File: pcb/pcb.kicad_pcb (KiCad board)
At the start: 2 copper layers, 34 parts, among them J1 USB_C_Receptacle_USB2.0_16P, J2 TC2030_SWD, J3 Conn_01x02_MountingPin, J4 Conn_01x04_MountingPin, SW1 SW_SPDT, SW2 RST, SW3 Kailh_Choc, SW4 Kailh_Choc, SW5 Kailh_Choc, SW6 Kailh_Choc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

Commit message: routing is hard
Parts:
- removed J2: TC2030_SWD, PCM_marbastlib-various:CON_TC2030_outlined
- J4: value Conn_01x04_MountingPin -> Conn_02x03_Odd_Even; footprint Connector_JST:JST_SH_SM04B-SRSS-TB_1x04-1MP_P1.00mm_Horizontal -> Connector_PinHeader_2.54mm:PinHeader_2x03_P2.54mm_Vertical
- moved F1 74.6 mm to (88.2, 51.6)
- moved FB2 71.3 mm to (86.4, 49.3), turned to -90 degrees
- moved SW3 69.4 mm to (30.0, 51.0)
- moved D1 68.7 mm to (92.4, 52.8), turned to -90 degrees
- moved SW6 67.4 mm to (30.0, 68.0)
- moved FB1 65.7 mm to (86.9, 53.6)
- moved U2 58.2 mm to (80.5, 52.5), turned to 180 degrees
- moved SW7 55.9 mm to (48.0, 68.0)
- moved SW8 53.7 mm to (66.0, 68.0)
- moved J4 46.4 mm to (96.4, 62.6)
- moved U1 43.7 mm to (86.8, 66.8)
- moved SW1 41.2 mm to (106.7, 56.0), turned to 90 degrees
- moved J1 39.8 mm to (80.5, 45.5), turned to 180 degrees
- moved R1 36.3 mm to (76.5, 52.5), turned to -90 degrees
- moved J3 34.1 mm to (104.2, 46.5)
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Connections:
- J4 pad 1: VBUS -> +3.3V
- J4 pad 2: /USB-D- -> /SWDIO
- J4 pad 3: /USB-D+ -> /RST
- J4 pad 4: GND -> /SWDCLK
- U1 pad 13: /SCL -> unconnected-(U1-P0.05-A-Pad13)
- U1 pad 15: /SDA -> unconnected-(U1-P0.07-Pad15)
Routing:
- net GND: track 0.00 -> 76.2 mm
- net /USB-D+: track 0.00 -> 49.2 mm
- net /USB-D-: track 0.00 -> 48.7 mm
- net /RST: track 0.00 -> 41.7 mm, vias 0 -> 1
- net GNDREF: track 0.00 -> 33.5 mm
- net VBUS: track 0.00 -> 13.2 mm
- net GNDPWR: track 0.00 -> 10.3 mm, vias 0 -> 2
- net /SWDIO: track 0.00 -> 8.12 mm
- net /SWDCLK: track 0.00 -> 6.49 mm
- net Net-(J1-CC1): track 0.00 -> 4.07 mm
- net Net-(J1-CC2): track 0.00 -> 3.73 mm
- net Net-(F1-Pad1): track 0.00 -> 1.99 mm
- net Net-(U3-CHRG): track 0.00 -> 1.43 mm
- net +BATT: track 0.00 -> 1.43 mm

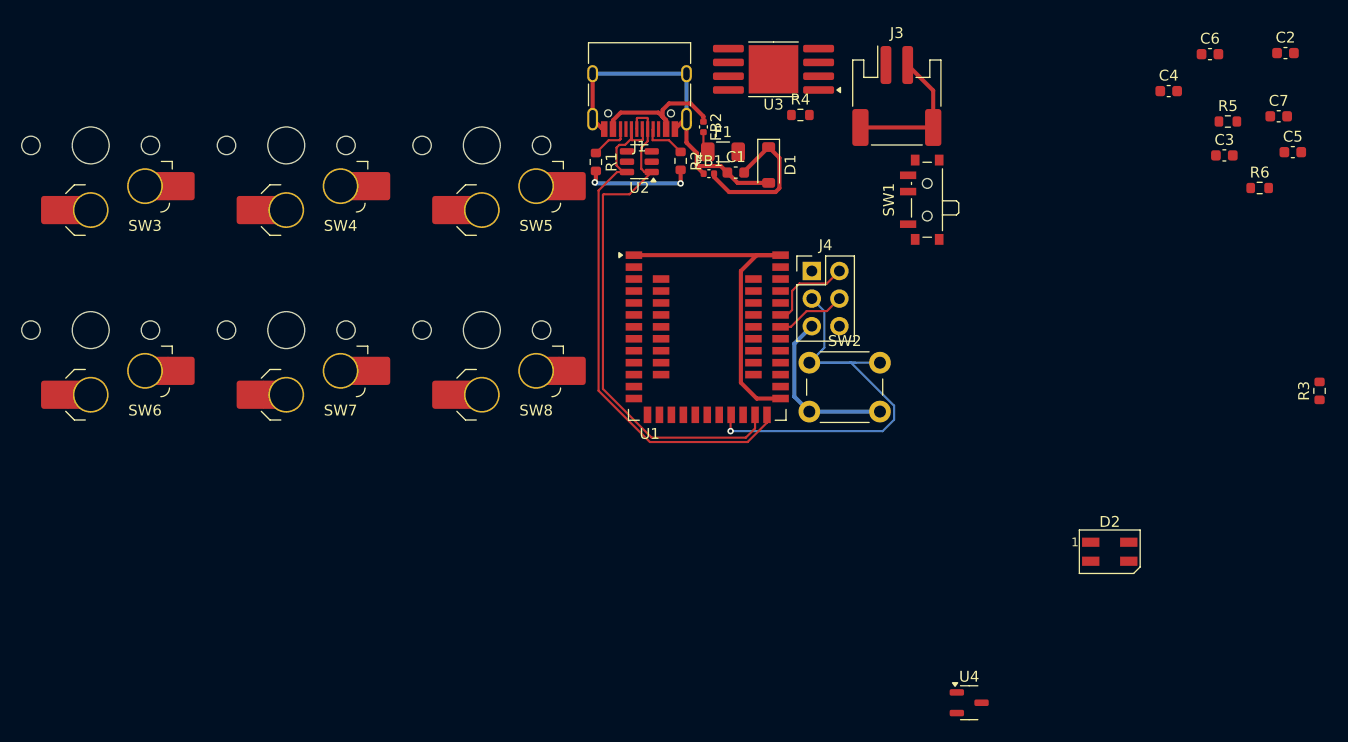
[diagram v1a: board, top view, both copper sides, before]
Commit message: finish routing first draft
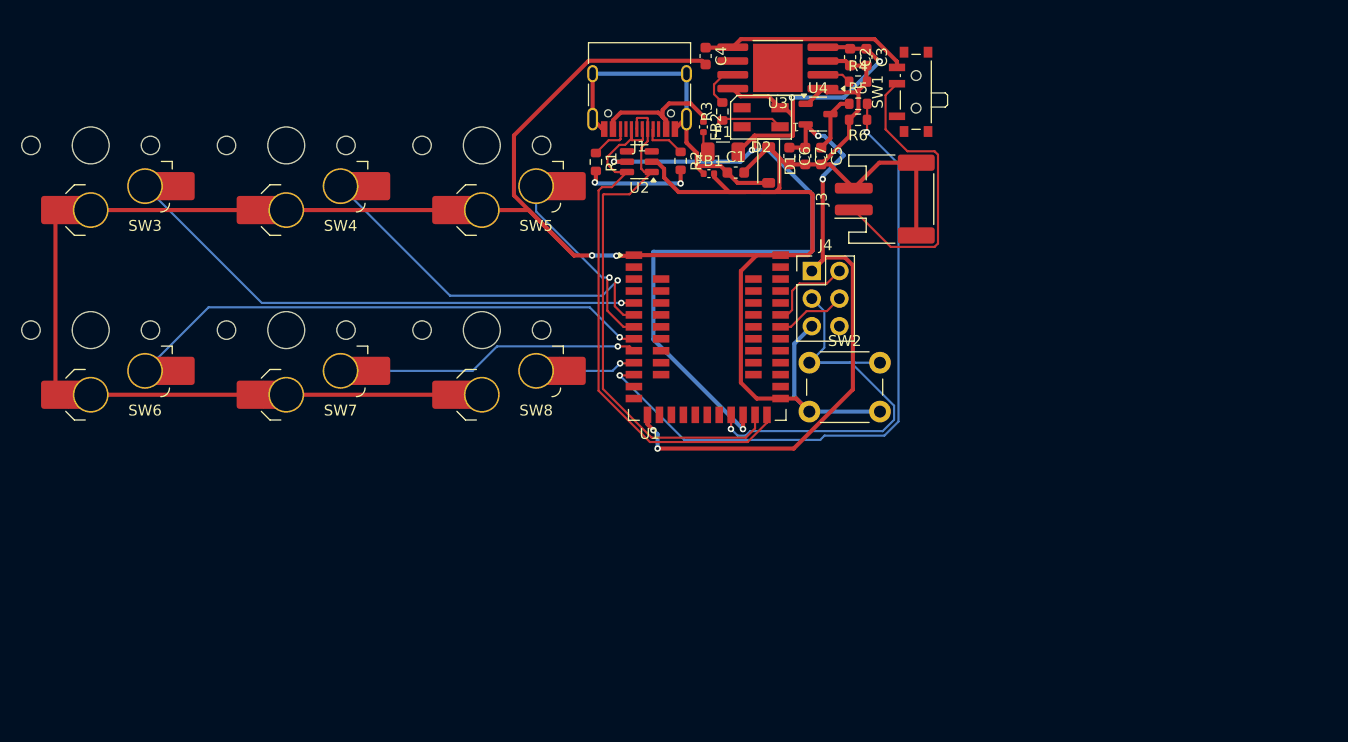
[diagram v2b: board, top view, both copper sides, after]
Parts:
- moved R3 60.7 mm to (88.1, 47.9)
- moved U4 55.9 mm to (97.0, 48.1)
- moved D2 51.3 mm to (91.7, 48.4), turned to 180 degrees
- moved C7 43.7 mm to (95.8, 52.0), turned to -90 degrees
- moved C5 43.4 mm to (97.2, 52.0), turned to -90 degrees
- moved C4 42.7 mm to (86.6, 42.8), turned to -90 degrees
- moved C2 40.1 mm to (99.9, 42.9), turned to -90 degrees
- moved C6 39.8 mm to (94.3, 52.0), turned to -90 degrees
- moved R6 37.5 mm to (100.6, 48.6), turned to 180 degrees
- moved C3 34.2 mm to (101.4, 42.9), turned to -90 degrees
- moved R5 34.1 mm to (100.6, 47.2)
- moved SW1 9.98 mm to (105.6, 46.1)
- moved J3 9.55 mm to (103.1, 55.9), turned to 90 degrees
- moved R4 6.13 mm to (100.6, 45.1)
- moved U3 0.42 mm to (93.2, 43.9)
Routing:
- net GND: track 76.2 -> 276.0 mm, vias 0 -> 2
- net +5V: track 0.00 -> 95.0 mm, vias 0 -> 5
- net /VSENSE: track 0.00 -> 60.8 mm, vias 0 -> 2
- net +3.3V: track 0.00 -> 59.9 mm, vias 0 -> 4
- net /sw3: track 0.00 -> 49.5 mm, vias 0 -> 1
- net /sw6: track 0.00 -> 48.6 mm, vias 0 -> 1
- net /sw4: track 0.00 -> 34.9 mm, vias 0 -> 1
- net /sw7: track 0.00 -> 28.1 mm, vias 0 -> 1
- net Net-(J3-Pin_1): track 0.00 -> 27.9 mm
- net +BATT: track 1.43 -> 19.3 mm
- net /sw5: track 0.00 -> 17.8 mm, vias 0 -> 1
- net /sw8: track 0.00 -> 9.31 mm, vias 0 -> 1
- net Net-(D2-K): track 0.00 -> 5.67 mm
- net +VSW: track 0.00 -> 5.56 mm
- net Net-(U3-PROG): track 0.00 -> 2.67 mm
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
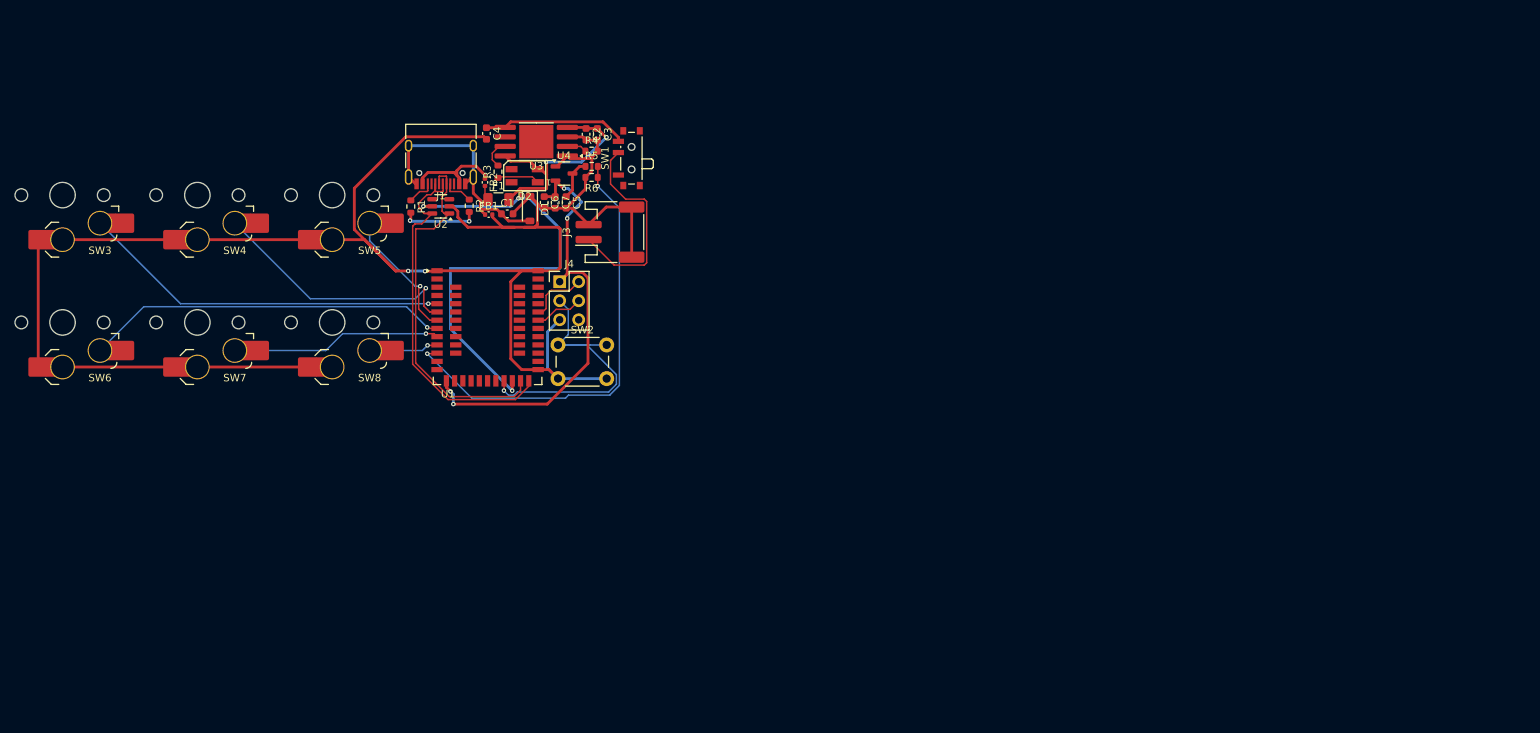
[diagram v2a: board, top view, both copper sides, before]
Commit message: one one gnd net, also get rid of some components
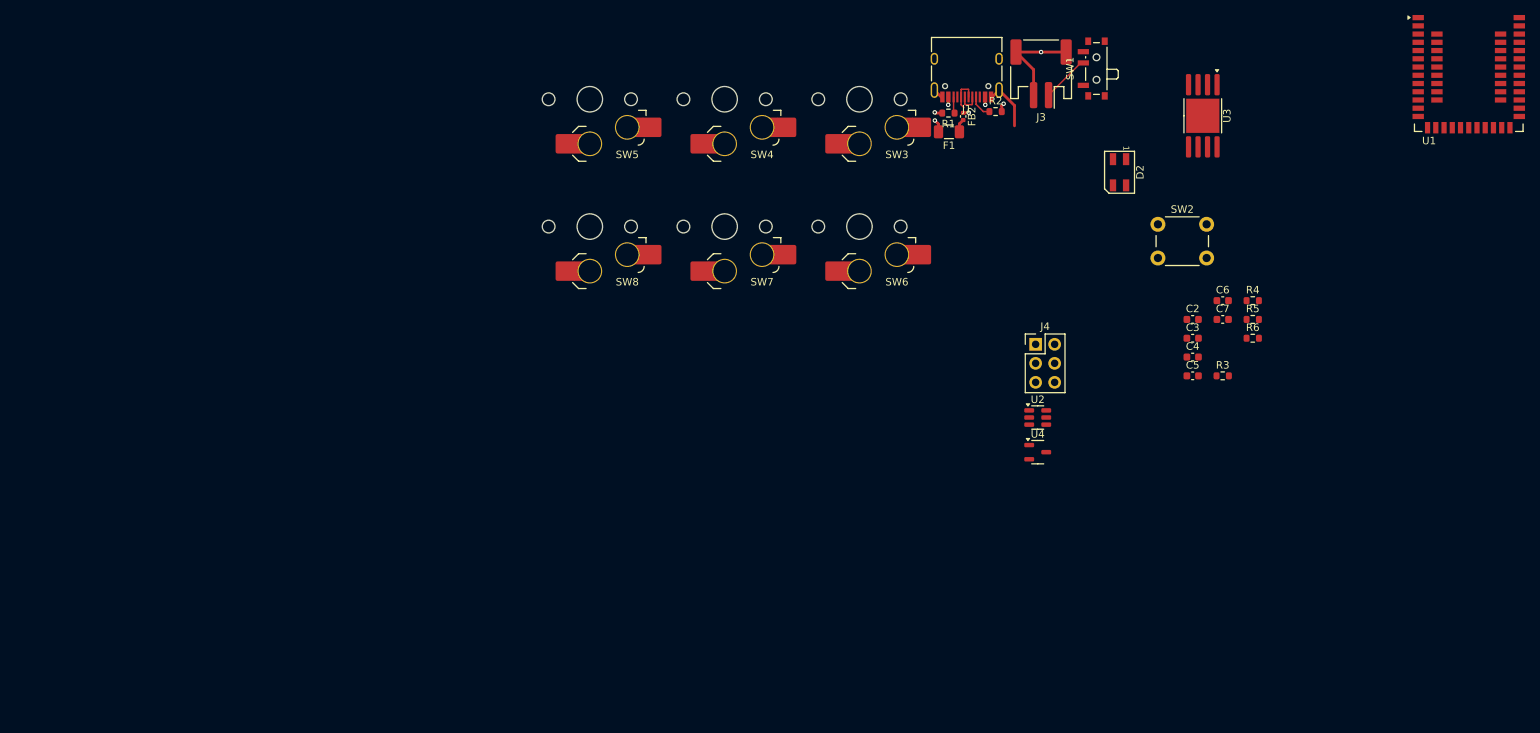
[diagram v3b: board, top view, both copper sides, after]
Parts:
- removed C1: 100n, Capacitor_SMD:C_0603_1608Metric
- removed D1: D_TVS, Diode_SMD:D_SOD-123
- removed FB1: FerriteBead_Small, Capacitor_SMD:C_0402_1005Metric
- moved U1 135.3 mm to (217.8, 33.0)
- moved SW3 107.2 mm to (136.4, 38.2)
- moved SW6 107.2 mm to (136.4, 55.2)
- moved R3 100.5 mm to (184.9, 75.1), turned to 0 degrees
- moved C4 98.9 mm to (180.9, 72.6), turned to 0 degrees
- moved C6 91.5 mm to (184.9, 65.1), turned to 0 degrees
- moved R6 90.8 mm to (188.9, 70.1), turned to 0 degrees
- moved R5 90.6 mm to (188.9, 67.6)
- moved R4 90.5 mm to (188.9, 65.1)
- moved C7 90.5 mm to (184.9, 67.6), turned to 0 degrees
- moved U3 89.1 mm to (182.2, 40.4), turned to -90 degrees
- moved C5 86.8 mm to (180.9, 75.1), turned to 0 degrees
- moved C2 84.7 mm to (180.9, 67.6), turned to 0 degrees
- moved U2 84.5 mm to (160.2, 80.7), turned to 0 degrees
- moved C3 84.0 mm to (180.9, 70.1), turned to 0 degrees
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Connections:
- J1 pad A1: GNDREF -> GND
- J1 pad A12: GNDREF -> GND
- J1 pad B1: GNDREF -> GND
- J1 pad B12: GNDREF -> GND
- J1 pad S1: GNDREF -> GND
- R1 pad 2: GNDPWR -> GND
- R2 pad 2: GNDPWR -> GND
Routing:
- net GND: track 276.0 -> 24.1 mm, vias 2 -> 3
- net +5V: track 95.0 -> 1.71 mm, vias 5 -> 1
- net /VSENSE: track 60.8 -> 0.00 mm, vias 2 -> 0
- net +3.3V: track 59.9 -> 0.00 mm, vias 4 -> 0
- net /sw3: track 49.5 -> 0.00 mm, vias 1 -> 0
- net /sw6: track 48.6 -> 0.00 mm, vias 1 -> 0
- net /USB-D+: track 51.2 -> 4.58 mm
- net /USB-D-: track 48.7 -> 2.99 mm
- net /RST: track 41.9 -> 0.00 mm, vias 1 -> 0
- net /sw4: track 34.9 -> 0.00 mm, vias 1 -> 0
- net GNDREF: track 33.5 -> 0.00 mm
- net /sw7: track 28.1 -> 0.00 mm, vias 1 -> 0
- net Net-(J3-Pin_1): track 27.9 -> 6.42 mm
- net +BATT: track 19.3 -> 0.00 mm
- net /sw5: track 17.8 -> 0.00 mm, vias 1 -> 0
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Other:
- copper layers 2 -> 4

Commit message: continue routing
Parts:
- SW3, SW4, SW5, SW6, SW7, SW8: moved to B.Cu
- moved U1 63.0 mm to (155.0, 38.8)
- moved U4 58.6 mm to (194.8, 38.1), turned to 180 degrees
- moved U3 44.1 mm to (220.8, 61.8)
- moved J4 36.9 mm to (164.4, 34.3)
- moved C5 36.9 mm to (205.5, 47.7), turned to 180 degrees
- moved D2 34.0 mm to (195.1, 72.0), turned to 90 degrees
- moved C4 33.3 mm to (205.5, 50.2), turned to 180 degrees
- moved R3 32.1 mm to (201.5, 47.7), turned to 180 degrees
- moved U2 31.9 mm to (148.6, 51.0)
- moved C3 30.2 mm to (205.5, 52.7), turned to 180 degrees
- moved C2 27.6 mm to (205.5, 55.2), turned to 180 degrees
- moved SW1 27.4 mm to (170.2, 61.4), turned to 0 degrees
- moved J1 25.7 mm to (151.2, 59.5), turned to 0 degrees
- moved J3 23.4 mm to (161.2, 58.2), turned to 0 degrees
- moved C7 20.7 mm to (201.5, 55.2), turned to 180 degrees
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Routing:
- net /USB-D-: track 2.99 -> 24.1 mm
- net /RST: track 0.00 -> 20.9 mm, vias 0 -> 1
- net /USB-D+: track 4.58 -> 22.1 mm
- net Net-(J3-Pin_1): track 6.42 -> 16.4 mm
- net /SWDIO: track 0.00 -> 7.94 mm
- net /SWDCLK: track 0.00 -> 6.40 mm
- net GND: track 24.1 -> 25.2 mm, vias 3 -> 1
- net +5V: track 1.71 -> 2.78 mm, vias 1 -> 2

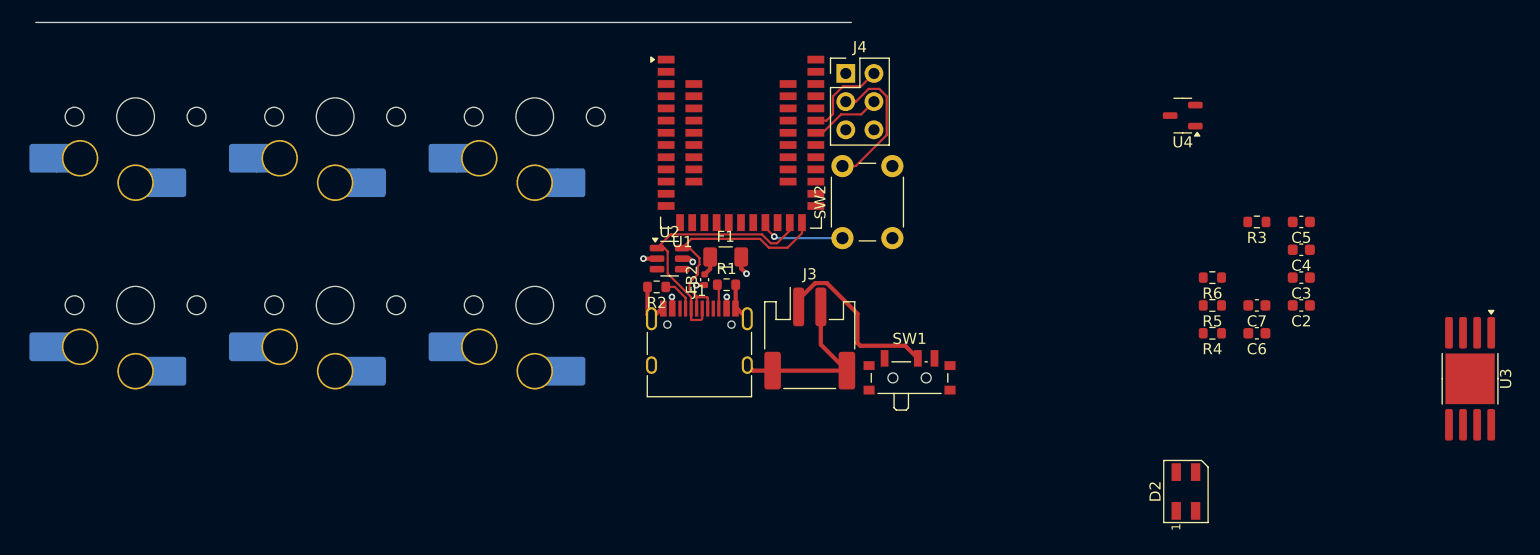
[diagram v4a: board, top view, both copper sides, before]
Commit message: finish routing 2nd draft
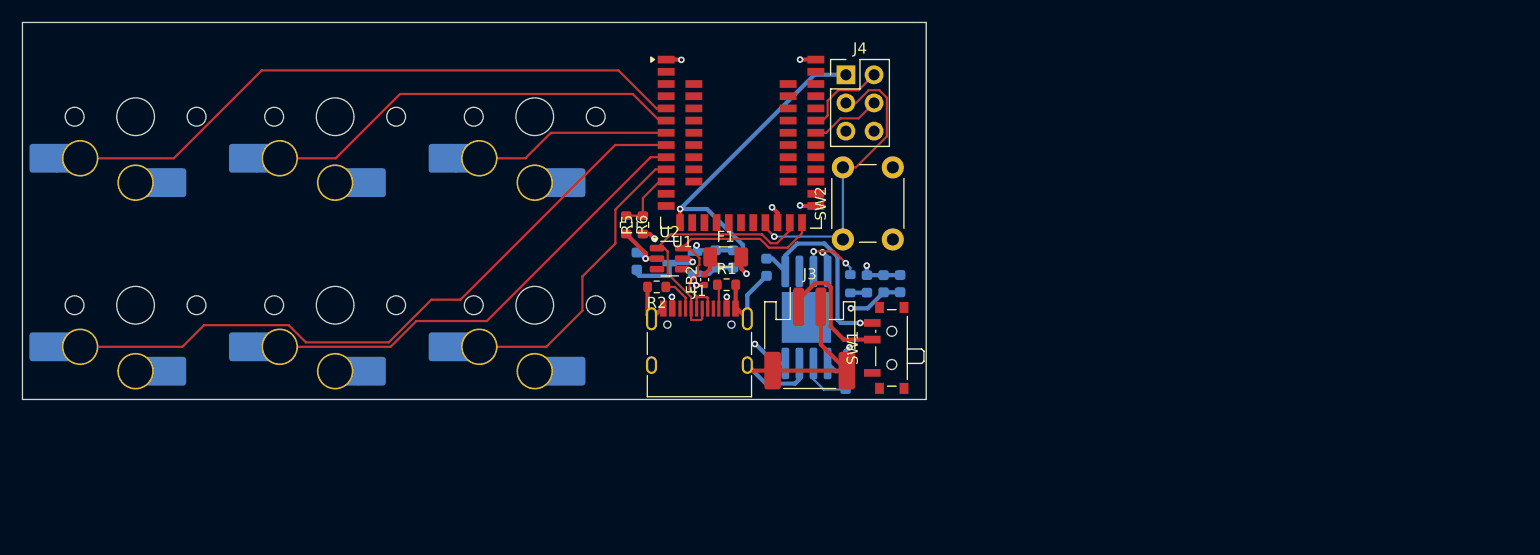
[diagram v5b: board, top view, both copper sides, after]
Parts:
- C2, C3, C4, C5, C6, C7, R3, R4, U3, U4: moved to B.Cu
- D2: footprint LED_SMD:LED_SK6812MINI_PLCC4_3.5x3.5mm_P1.75mm -> LED_SMD:LED_0603_1608Metric; moved to B.Cu
- moved U3 60.1 mm to (160.9, 56.3), turned to 90 degrees
- moved C5 60.0 mm to (145.6, 51.2), turned to 90 degrees
- moved R6 53.1 mm to (144.7, 48.0), turned to -90 degrees
- moved R5 51.9 mm to (146.2, 48.0), turned to 90 degrees
- moved C6 49.3 mm to (152.7, 51.0), turned to 90 degrees
- moved C4 48.3 mm to (157.3, 51.8), turned to -90 degrees
- moved C7 47.4 mm to (154.3, 51.0), turned to 90 degrees
- moved U4 47.0 mm to (149.7, 51.4)
- moved C3 37.7 mm to (167.9, 53.3), turned to -90 degrees
- moved R3 37.1 mm to (164.9, 53.3), turned to 90 degrees
- moved C2 36.2 mm to (169.3, 53.3), turned to -90 degrees
- moved SW5 36.0 mm to (136.4, 38.2)
- moved SW6 36.0 mm to (100.4, 55.2)
- moved SW8 36.0 mm to (136.4, 55.2)
- moved SW3 36.0 mm to (100.4, 38.2)
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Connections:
- C5 pad 1: +VSW -> +5V
- R5 pad 1: +VSW -> +5V
- U4 pad 3: +VSW -> +5V
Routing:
- net /sw6: track 0.00 -> 61.7 mm
- net /sw3: track 0.00 -> 57.5 mm
- net /sw7: track 0.00 -> 41.9 mm
- net /sw4: track 0.00 -> 38.2 mm
- net +3.3V: track 0.00 -> 34.3 mm, vias 0 -> 1
- net GND: track 25.2 -> 58.3 mm, vias 1 -> 7
- net /sw8: track 0.00 -> 27.1 mm
- net +5V: track 2.78 -> 25.9 mm, vias 2 -> 7
- net +BATT: track 0.00 -> 18.2 mm, vias 0 -> 1
- net /sw5: track 0.00 -> 17.8 mm
- net /RST: track 20.9 -> 27.6 mm
- net Net-(U3-CHRG): track 0.00 -> 6.35 mm, vias 0 -> 2
- net /VSENSE: track 0.00 -> 5.80 mm
- net Net-(U3-PROG): track 0.00 -> 4.70 mm
- net Net-(J3-Pin_1): track 16.4 -> 12.1 mm
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- added copper zone on In2.Cu, net +5V
- added copper zone on In1.Cu, net GND
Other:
- board outline added: 81.5 x 34 mm

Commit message: update ground and 5v pours to cover the whole board
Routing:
- net +5V: track 25.9 -> 21.4 mm
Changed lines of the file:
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@@
-		(net 2)
-	)
-	(segment
-		(start 162.570486 50.661)
-		(end 165.371 50.661)
-		(width 0.38)
-		(layer "In2.Cu")
-		(net 2)
-	)
-	(segment
-		(start 162.345377 50.435891)
-		(end 162.570486 50.661)
-		(width 0.38)
-		(layer "In2.Cu")
-		(net 2)
-	)
-	(segment
-		(start 165.371 50.661)
-		(end 166.34 51.63)
-		(width 0.38)
-		(layer "In2.Cu")
 		(net 2)
 	)
@@
 		(polygon
 			(pts
-				(xy 168.775 32.65) (xy 91.175 32.75) (xy 90.975 63.575) (xy 170.75 63.225) (xy 170.75 32.65)
+				(xy 171.7 29.7) (xy 164.55 29.7) (xy 164.55 32.575) (xy 145.475 32.6) (xy 145.475 29.7) (xy 90.2 29.7)
+				(xy 90.2 63.7) (xy 171.7 63.7)
 			)
 		)
@@
 		(polygon
 			(pts
-				(xy 170.75 63.225) (xy 145.925 63.325) (xy 145.925 45.475) (xy 170.775 45.45)
+				(xy 171.7 29.7) (xy 164.55 29.7) (xy 164.55 32.575) (xy 145.45 32.575) (xy 145.45 29.7) (xy 90.2 29.7)
+				(xy 90.2 63.7) (xy 171.7 63.7)
 			)
 		)
